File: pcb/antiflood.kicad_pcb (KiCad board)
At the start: 2 copper layers, 88 x 84 mm, 94 parts, among them J1 Barrel_Jack, J10 Screw_Terminal_01x02, J11 Screw_Terminal_01x02, J12 Screw_Terminal_01x02, J13 Screw_Terminal_01x02, J2 Conn_01x03_Male, J3 01x03, J4 01x03, J5 Conn_02x04_Odd_Even, J6 Conn_02x05_Odd_Even, J7 Conn_02x03_Odd_Even, J8 Screw_Terminal_01x02, J9 Screw_Terminal_01x02, K1 P-5, K2 P-5, Q1 2N3904, Q2 2N3904, SW1 SW_Push, SW2 SW_Push, SW3 SW_Push, U1 ATMEGA328P-AU, U2 TL7705, U3 LM1117-3.3, U4 MT3608, U5 MC34063, U6 TP4056, Y1 16MHz

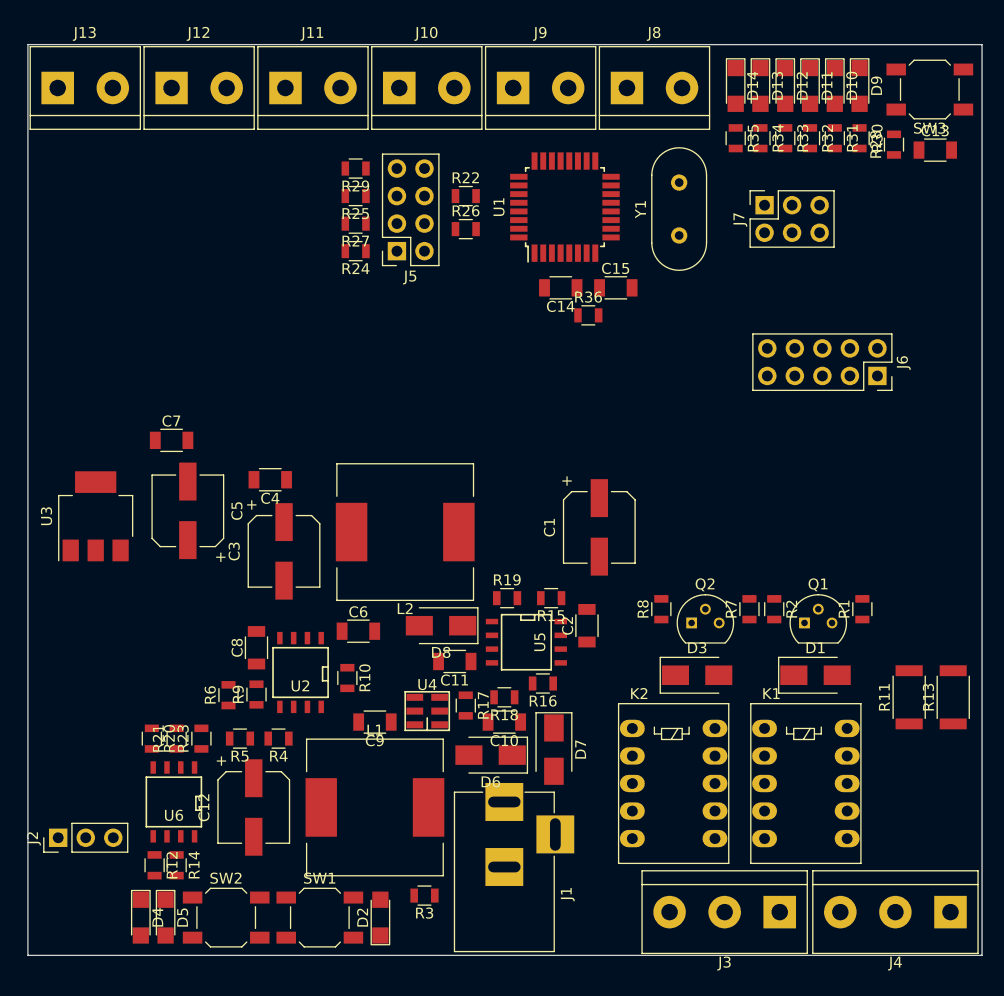
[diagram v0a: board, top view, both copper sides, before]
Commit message: PCB: smd transistors, components placement
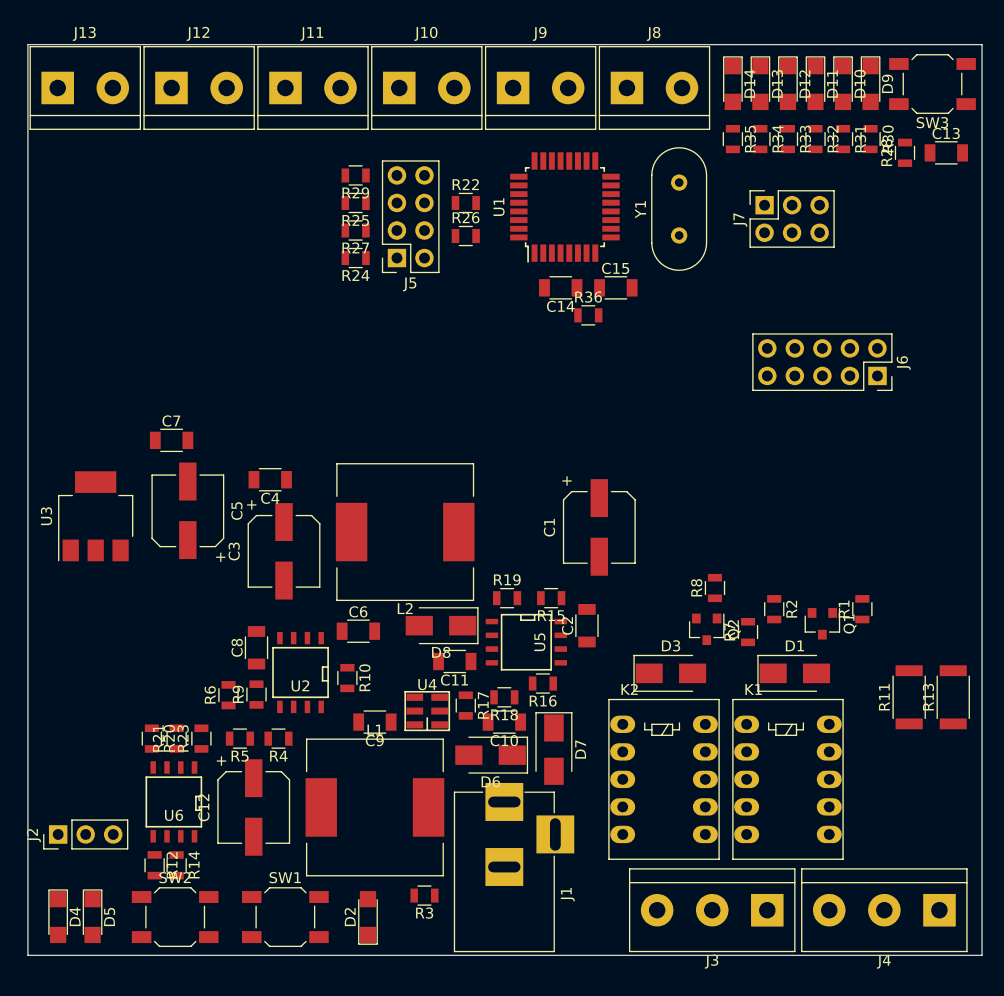
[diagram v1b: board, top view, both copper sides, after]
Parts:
- Q1, Q2: value 2N3904 -> MMBT3904; footprint TO_SOT_Packages_THT:TO-92_Molded_Narrow -> TO_SOT_Packages_SMD:SOT-23
- moved D4 7.62 mm to (74.3, 131.4)
- moved D5 6.74 mm to (77.5, 131.4)
- moved R8 5.32 mm to (134.9, 101.1)
- moved SW2 4.70 mm to (85.1, 131.4)
- moved SW1 3.18 mm to (95.2, 131.4)
- moved D3 2.42 mm to (130.8, 109.0)
- moved R7 2.12 mm to (137.9, 105.2)
- moved D1 1.92 mm to (142.2, 109.0)
- moved K1 1.69 mm to (137.8, 113.7)
- moved Q1 1.65 mm to (144.8, 104.4), turned to 270 degrees
- moved Q2 1.51 mm to (134.1, 104.9), turned to 270 degrees
- moved R28 1.27 mm to (152.4, 61.0)
- moved J3 1.16 mm to (139.7, 130.8)
- moved D2 1.15 mm to (102.9, 131.4)
- moved C13 1.05 mm to (156.2, 61.0)
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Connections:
- Q1 pad 1: GND -> Net-(Q1-Pad1)
- Q1 pad 2: Net-(Q1-Pad2) -> GND
- Q2 pad 1: GND -> Net-(Q2-Pad1)
- Q2 pad 2: Net-(Q2-Pad2) -> GND
- R2 pad 2: Net-(Q1-Pad2) -> Net-(Q1-Pad1)
- R8 pad 1: Net-(Q2-Pad2) -> Net-(Q2-Pad1)

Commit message: PCB: placement before tracks
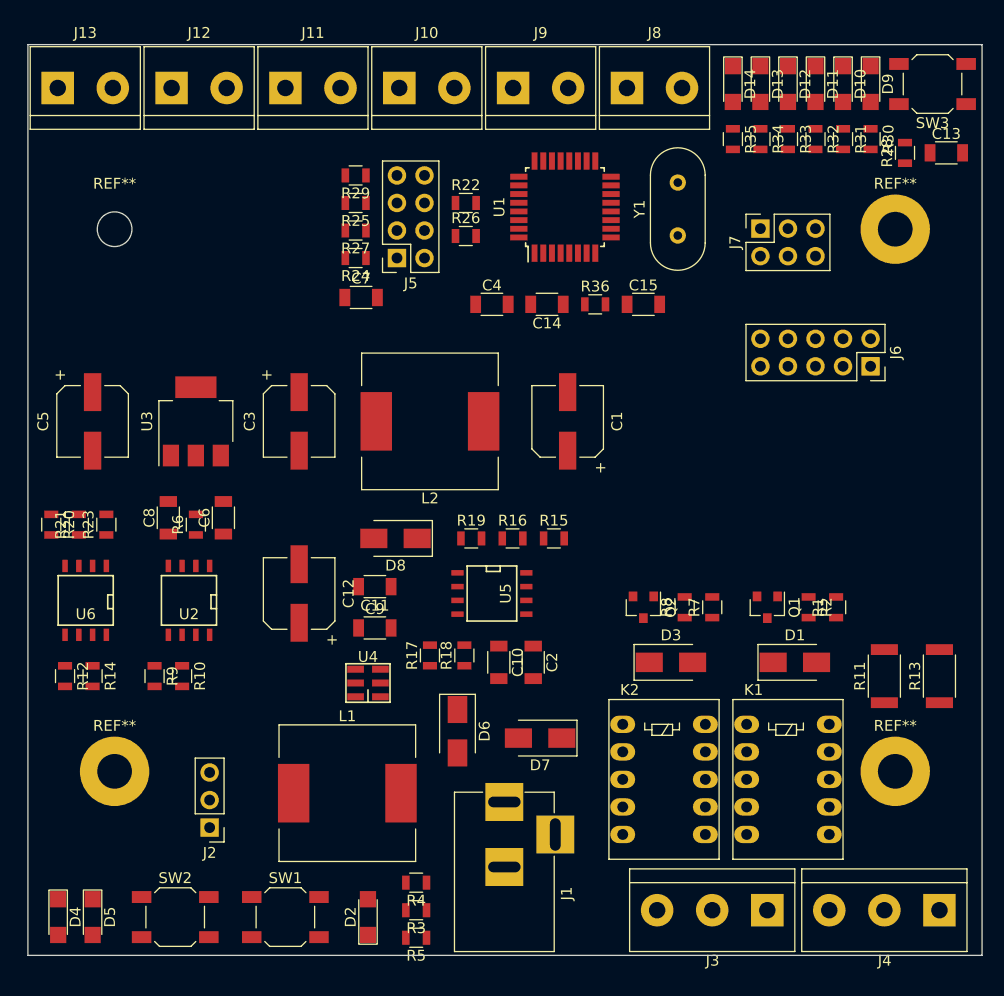
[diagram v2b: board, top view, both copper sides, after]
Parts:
- added REF**: MountingHole_3.2mm_M3_Pad, Mounting_Holes:MountingHole_3.2mm_M3_Pad, F.Cu at (151.5, 68.0)
- added REF**: MountingHole_3.2mm_M3, Mounting_Holes:MountingHole_3.2mm_M3, F.Cu at (79.5, 68.0)
- added REF**: MountingHole_3.2mm_M3_Pad, Mounting_Holes:MountingHole_3.2mm_M3_Pad, F.Cu at (151.5, 118.0)
- added REF**: MountingHole_3.2mm_M3_Pad, Mounting_Holes:MountingHole_3.2mm_M3_Pad, F.Cu at (79.5, 118.0)
- moved C4 26.1 mm to (114.3, 74.9), turned to 0 degrees
- moved R5 24.5 mm to (107.3, 133.3)
- moved C7 21.9 mm to (102.2, 74.3)
- moved R20 21.8 mm to (73.7, 95.2)
- moved R21 21.7 mm to (76.2, 95.2)
- moved R23 21.6 mm to (78.7, 95.2)
- moved U6 20.3 mm to (76.8, 102.2)
- moved C12 20.2 mm to (96.5, 101.6), turned to 90 degrees
- moved R12 19.3 mm to (74.9, 109.2)
- moved R14 19.1 mm to (77.5, 109.2)
- moved R4 18.4 mm to (107.3, 128.3)
- moved C6 16.3 mm to (89.5, 94.6), turned to 90 degrees
- moved R6 16.0 mm to (87.0, 95.2)
- moved R10 15.2 mm to (85.7, 109.2)
- moved C8 14.5 mm to (84.5, 94.6)
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
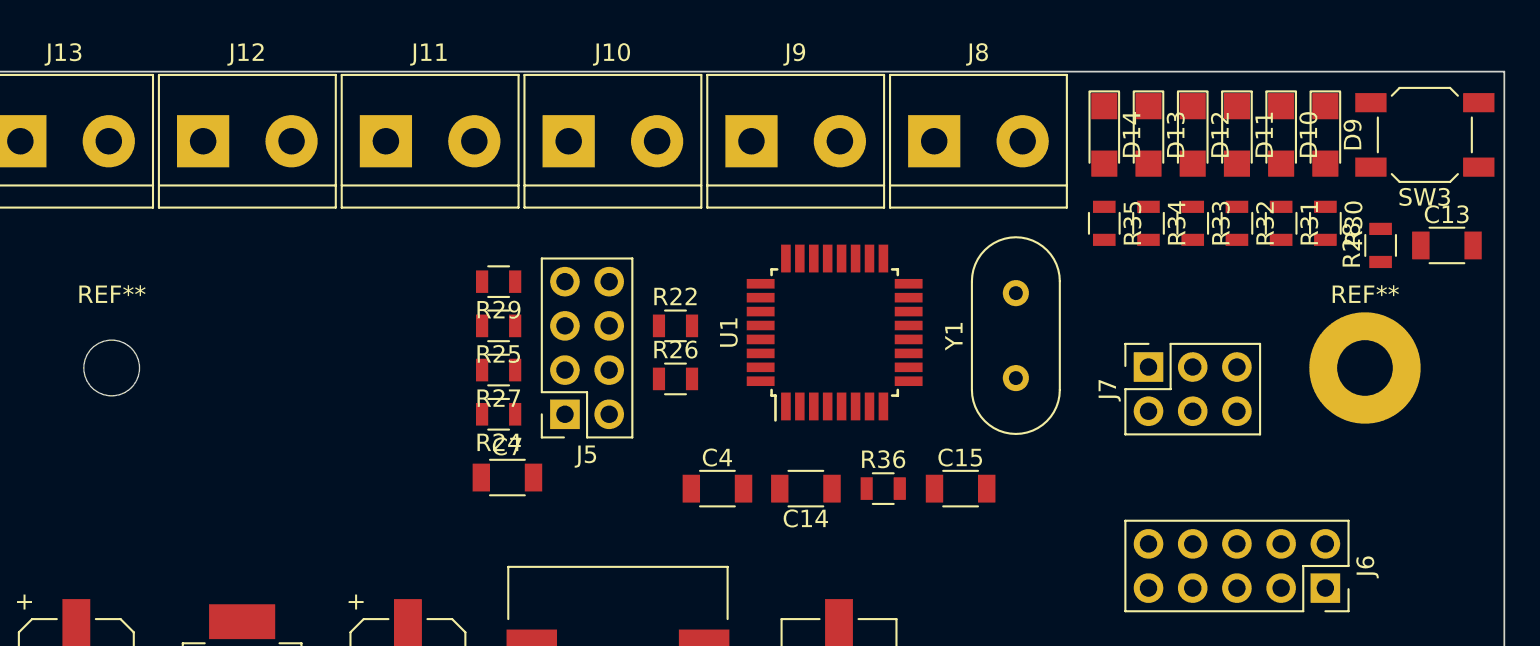
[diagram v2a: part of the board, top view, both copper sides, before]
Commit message: PCB: start tracks
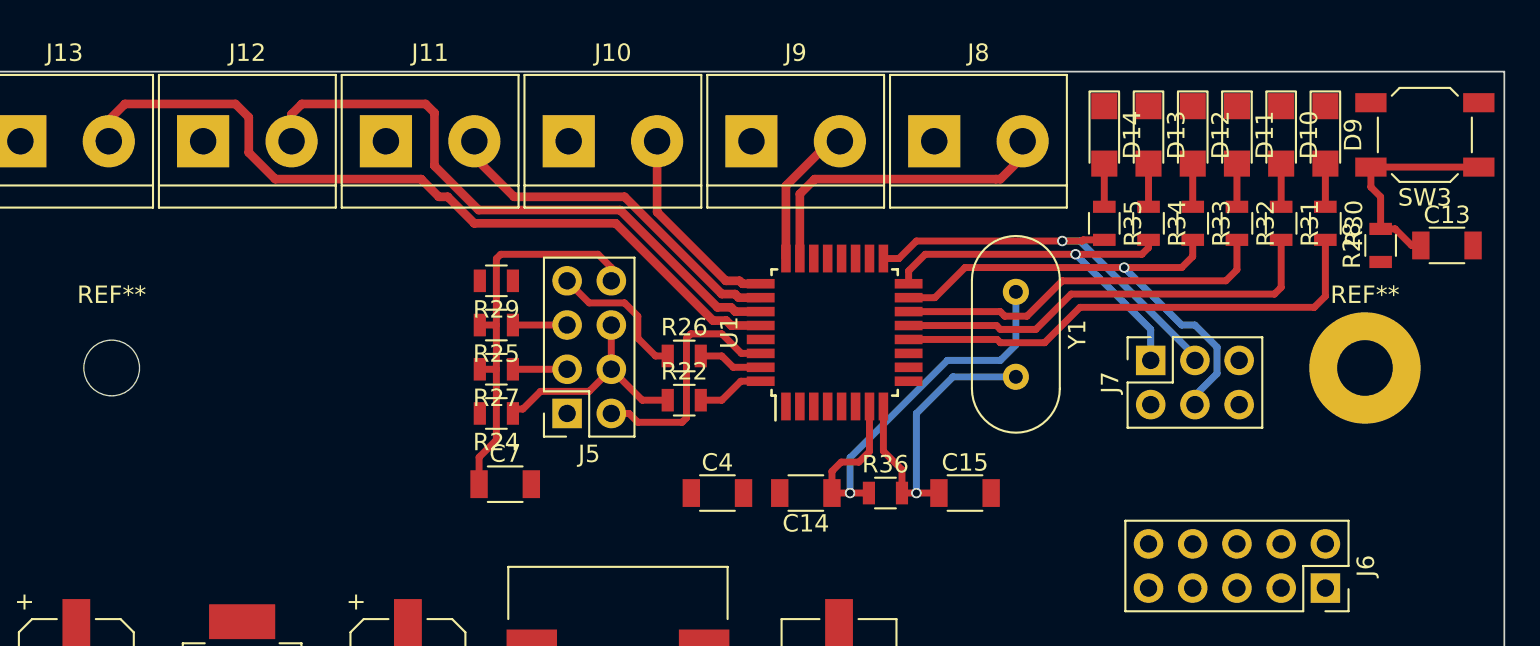
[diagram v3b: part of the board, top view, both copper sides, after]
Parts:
- moved Y1 4.95 mm to (131.4, 63.6), turned to 270 degrees
- moved R22 4.30 mm to (112.4, 69.8)
- moved R26 1.41 mm to (112.4, 67.3)
- moved J7 0.40 mm to (139.2, 67.6)
- moved C7 0.40 mm to (102.1, 74.7)
- moved C15 0.36 mm to (128.5, 75.2)
- moved R36 0.28 mm to (124.0, 75.2)
- moved C14 0.25 mm to (119.4, 75.2)
- moved C4 0.25 mm to (114.3, 75.2)
- moved R24 0.14 mm to (101.6, 70.6)
- moved R25 0.14 mm to (101.6, 65.5)
- moved R27 0.14 mm to (101.6, 68.1)
- moved R29 0.14 mm to (101.6, 63.0)
- moved J5 0.13 mm to (105.7, 70.6)
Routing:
- net /A5: track 0.00 -> 45.5 mm
- net /A4: track 0.00 -> 35.5 mm
- net /L3: track 0.00 -> 29.3 mm, vias 0 -> 1
- net /L0: track 0.00 -> 28.4 mm
- net /O1: track 0.00 -> 25.9 mm, vias 0 -> 1
- net /L1: track 0.00 -> 25.2 mm
- net /L5: track 0.00 -> 23.7 mm, vias 0 -> 1
- net /L4: track 0.00 -> 23.4 mm, vias 0 -> 1
- net +3V3: track 0.00 -> 23.1 mm
- net /DBG: track 0.00 -> 21.8 mm
- net /A3: track 0.00 -> 20.7 mm
- net /O2: track 0.00 -> 18.7 mm, vias 0 -> 1
- net /A0: track 0.00 -> 18.3 mm
- net /WRX: track 0.00 -> 14.0 mm
- net Net-(J5-Pad4): track 0.00 -> 13.2 mm
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
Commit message: PCB: tracking
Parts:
- moved J6 10.8 mm to (139.2, 76.7), turned to 90 degrees
- moved SW1 10.2 mm to (85.1, 131.4)
- moved SW2 9.52 mm to (94.6, 131.4)
- moved K1 0.25 mm to (137.5, 113.7)
- moved C10 0.13 mm to (115.1, 108.0), turned to 90 degrees
- turned C2 to 90 degrees
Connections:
- U1 pad 10: /PCL -> /PON
- U1 pad 11: /PON -> /FON
- U1 pad 2: /FON -> /PCL
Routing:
- net +5V: track 0.00 -> 340.4 mm, vias 0 -> 4
- net /A6: track 0.00 -> 151.7 mm, vias 0 -> 2
- net /BAT: track 0.00 -> 91.5 mm
- net Net-(D1-Pad2): track 0.00 -> 91.0 mm, vias 0 -> 1
- net +12V: track 0.00 -> 83.1 mm
- net /BSTE: track 0.00 -> 70.2 mm, vias 0 -> 3
- net Net-(D3-Pad2): track 0.00 -> 69.8 mm, vias 0 -> 1
- net /RST: track 12.7 -> 75.7 mm, vias 0 -> 1
- net /A7: track 0.00 -> 52.2 mm, vias 0 -> 2
- net /FON: track 0.00 -> 50.2 mm
- net /PON: track 0.00 -> 46.9 mm
- net /EPWR: track 0.00 -> 43.8 mm, vias 0 -> 2
- net +3V3: track 23.1 -> 64.5 mm
- net /PCL: track 0.00 -> 41.1 mm
- net /BTMP: track 0.00 -> 38.2 mm, vias 0 -> 1
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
